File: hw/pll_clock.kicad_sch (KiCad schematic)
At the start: 21 parts, among them J7 BNC, U7 5P49V5925, Y1 26MHz

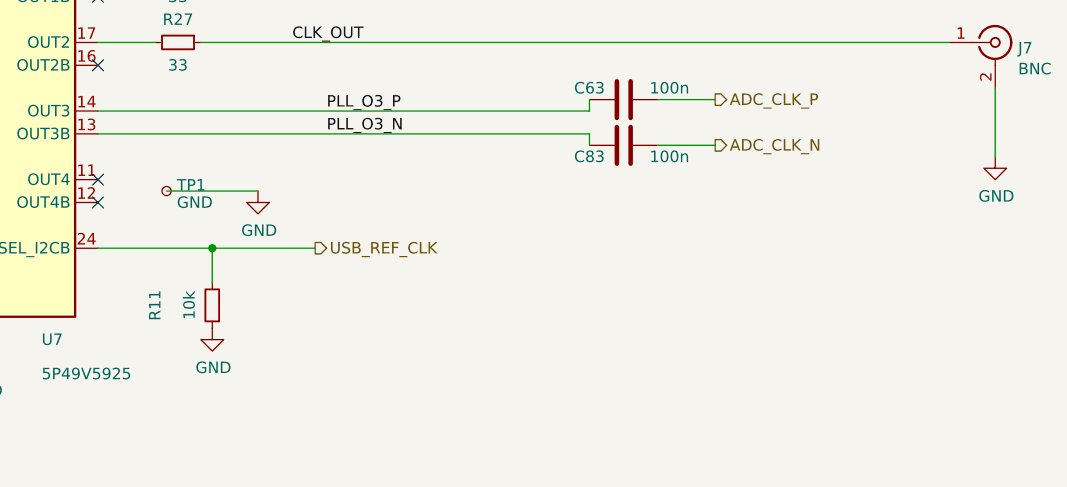
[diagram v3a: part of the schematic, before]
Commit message: finished routing; DRC passes (except for 1 hole violation at push-button)
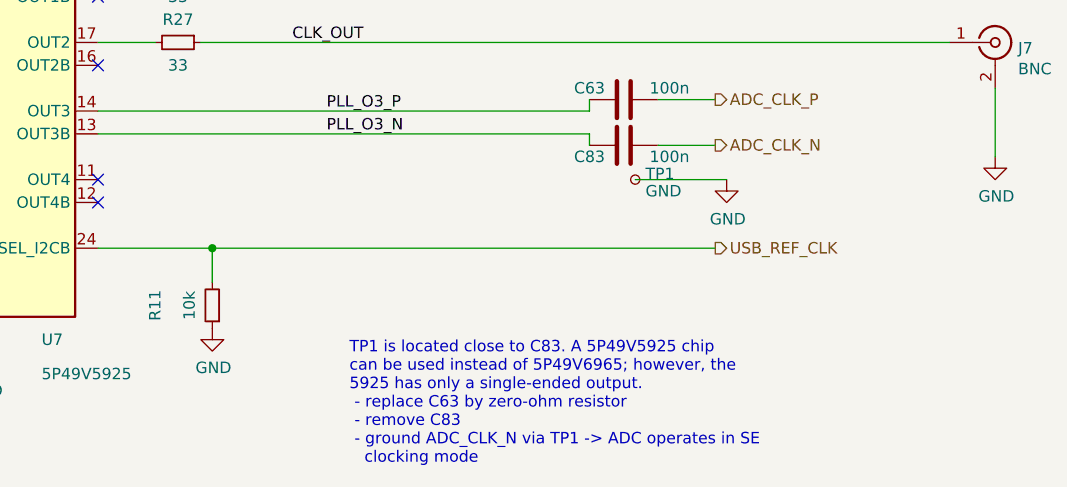
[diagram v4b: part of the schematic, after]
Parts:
- C18, C40, C41, C42, C43, C44, C45, C63, C83: Manufacturer Murata -> (none); Part GCJ188R71E104KA12D -> (none)
- C19, C46, C47: Manufacturer Murata -> (none); Part GCJ219R71C105KA01 -> (none)
- C48: Manufacturer TDK -> (none); Part CNC5L1X7R1C106K160AE -> (none)
- R11: Manufacturer Yageo -> (none); Part RT0603FRE0710KL -> (none)
- R24, R27: Manufacturer Yageo -> (none); Part RC0603FR-0733RL -> (none)
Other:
- note added: "TP1 is located close to C83. A 5P49V5925 chip can be used instead of 5P49V6965; however, the 5925 has only a single-ended output. - replace C63 by zero-ohm resistor - remove C83 - ground ADC_CLK_N via TP1 -> ADC operates in SE clocking mode"
- moved on the sheet: TP1

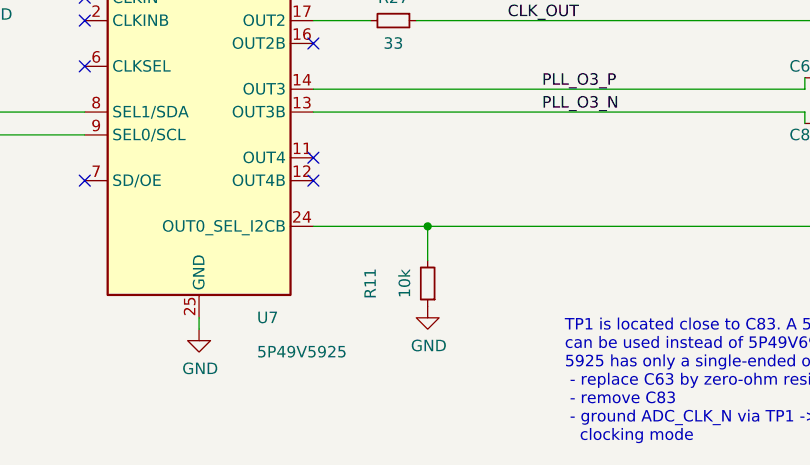
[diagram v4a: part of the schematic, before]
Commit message: standardized resistor/capacitor values
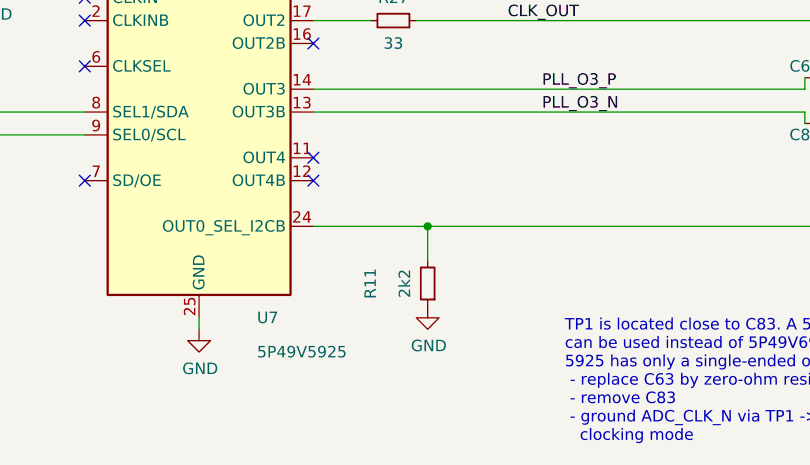
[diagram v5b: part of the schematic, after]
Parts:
- R11: value 10k -> 2k2
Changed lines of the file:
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@@
       (effects (font (size 1.27 1.27)))
     )
-    (property "Value" "10k" (at 165.1 110.49 90)
+    (property "Value" "2k2" (at 165.1 110.49 90)
       (effects (font (size 1.27 1.27)))
     )

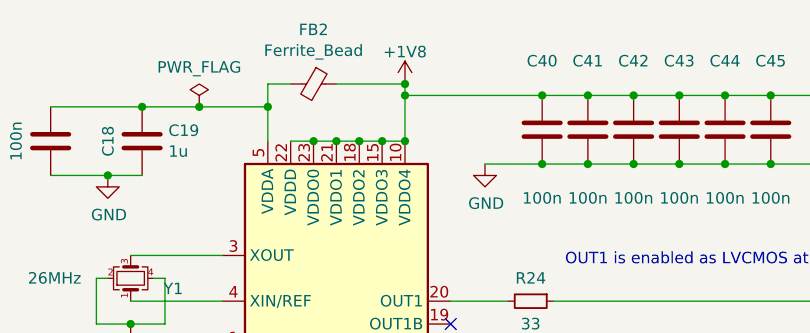
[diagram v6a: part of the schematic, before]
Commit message: moved trion into place; going to 'hide' footprint reference designators...
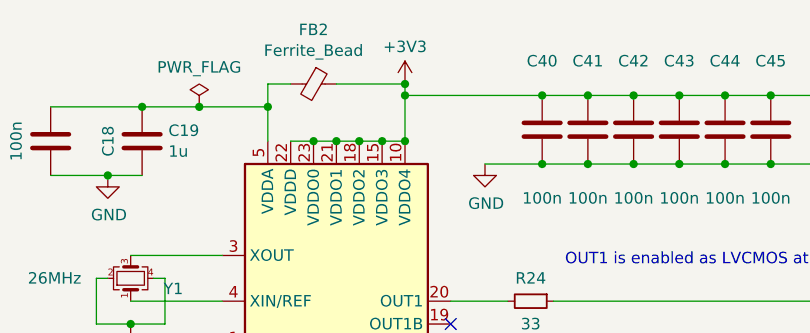
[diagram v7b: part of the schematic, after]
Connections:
- net +1V8 renamed +3V3
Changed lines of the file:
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@@
   (junction (at 175.26 58.42) (diameter 0) (color 0 0 0 0)
   )
+  (junction (at 142.24 55.88) (diameter 0) (color 0 0 0 0)
+  )
+  (junction (at 167.64 104.14) (diameter 0) (color 0 0 0 0)
+  )
+  (junction (at 204.47 50.8) (diameter 0) (color 0 0 0 0)
+  )
+  (junction (at 134.62 52.07) (diameter 0) (color 0 0 0 0)
+  )
+  (junction (at 180.34 58.42) (diameter 0) (color 0 0 0 0)
+  )
+  (junction (at 170.18 50.8) (diameter 0) (color 0 0 0 0)
+  )
+  (junction (at 165.1 58.42) (diameter 0) (color 0 0 0 0)
+  )
+  (junction (at 116.84 59.69) (diameter 0) (color 0 0 0 0)
+  )
   (junction (at 149.86 49.53) (diameter 0) (color 0 0 0 0)
-  )
-  (junction (at 142.24 55.88) (diameter 0) (color 0 0 0 0)
-  )
-  (junction (at 167.64 104.14) (diameter 0) (color 0 0 0 0)
-  )
-  (junction (at 204.47 50.8) (diameter 0) (color 0 0 0 0)
-  )
-  (junction (at 134.62 52.07) (diameter 0) (color 0 0 0 0)
-  )
-  (junction (at 180.34 58.42) (diameter 0) (color 0 0 0 0)
-  )
-  (junction (at 170.18 50.8) (diameter 0) (color 0 0 0 0)
-  )
-  (junction (at 165.1 58.42) (diameter 0) (color 0 0 0 0)
-  )
-  (junction (at 116.84 59.69) (diameter 0) (color 0 0 0 0)
   )
   (junction (at 185.42 58.42) (diameter 0) (color 0 0 0 0)
@@
         (path "/7c8a1f8d-8834-4c9b-aaae-1f231e9b09a1/00000000-0000-0000-0000-000060b16d71"
           (reference "#PWR0118") (unit 1)
-        )
-      )
-    )
-  )
-  (symbol (lib_id "power:+1V8") (at 149.86 49.53 0) (unit 1)
-    (in_bom yes) (on_board yes) (dnp no)
-    (property "Reference" "#PWR0115" (at 149.86 53.34 0)
-      (effects (font (size 1.27 1.27)) hide)
-    )
-    (property "Value" "+1V8" (at 149.86 45.974 0)
-      (effects (font (size 1.27 1.27)))
-    )
-    (property "Footprint" "" (at 149.86 49.53 0)
-      (effects (font (size 1.27 1.27)) hide)
-    )
-    (property "Datasheet" "" (at 149.86 49.53 0)
-      (effects (font (size 1.27 1.27)) hide)
-    )
-    (pin "1")
-    (instances
-      (project "usbadc"
-        (path "/7c8a1f8d-8834-4c9b-aaae-1f231e9b09a1/00000000-0000-0000-0000-000060b16d71"
-          (reference "#PWR0115") (unit 1)
         )
       )
@@
         )
       )
+    )
+  )
+  (symbol (lib_id "power:+3V3") (at 149.86 49.53 0) (unit 1)
+    (in_bom yes) (on_board yes) (dnp no) (fields_autoplaced)
+    (property "Reference" "#PWR098" (at 149.86 53.34 0)
+      (effects (font (size 1.27 1.27)) hide)
+    )
+    (property "Value" "+3V3" (at 149.86 45.3969 0)
+      (effects (font (size 1.27 1.27)))
+    )
+    (property "Footprint" "" (at 149.86 49.53 0)
+      (effects (font (size 1.27 1.27)) hide)
+    )
+    (property "Datasheet" "" (at 149.86 49.53 0)
+      (effects (font (size 1.27 1.27)) hide)
+    )
+    (pin "1")
+    (instances
+      (project "usbadc"
+        (path "/7c8a1f8d-8834-4c9b-aaae-1f231e9b09a1/00000000-0000-0000-0000-000060b16d71"
+          (reference "#PWR098") (unit 1)
+        )
+      )

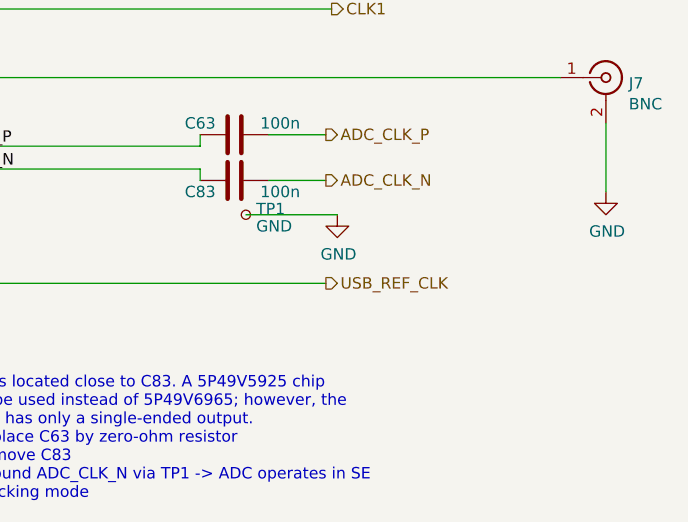
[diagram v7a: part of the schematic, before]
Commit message: layout almost complete with UPLI on the RHS => NO CLOCK INPUT
Have to rework and move the usb transceiver to the left...
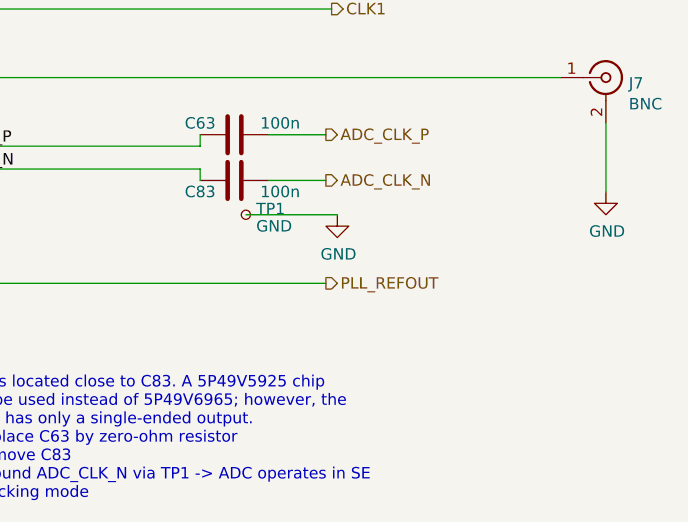
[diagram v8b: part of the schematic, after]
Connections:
- net USB_REF_CLK renamed PLL_REFOUT
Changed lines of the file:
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@@
     (effects (font (size 1.27 1.27)) (justify left))
   )
-  (hierarchical_label "USB_REF_CLK" (shape output) (at 223.52 104.14 0) (fields_autoplaced)
+  (hierarchical_label "PLL_REFOUT" (shape output) (at 223.52 104.14 0) (fields_autoplaced)
     (effects (font (size 1.27 1.27)) (justify left))
   )
